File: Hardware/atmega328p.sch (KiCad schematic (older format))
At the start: 21 parts, among them J401 USART, Q001 Q_NPN_Darlington_BEC, U401 ATMEGA328P-PU, Y401 16MHz

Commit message: Atualização do MIC19
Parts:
- added RV401: 1K, Potentiometer_THT:Potentiometer_Bourns_3296W_Vertical, symbol Device:R_POT_TRIM
- BZ1: renamed from BZ001; footprint (none) -> Buzzer_Beeper:Buzzer_12x9.5RM7.6
- C407: footprint (none) -> Capacitor_SMD:C_0805_2012Metric_Pad1.15x1.40mm_HandSolder
- D402: value BYC77 -> BYD77; footprint (none) -> Diode_SMD:D_MiniMELF_Handsoldering
- Q101: renamed from Q001; value Q_NPN_Darlington_BEC -> BCV27; footprint (none) -> Package_TO_SOT_SMD:SOT-23_Handsoldering
- R404, R405, R406: footprint (none) -> Resistor_SMD:R_0805_2012Metric_Pad1.15x1.40mm_HandSolder
- renumbered D402 to D403
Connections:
- net +5V: now also R406.1, RV401.3; no longer BZ1.2 (+), D402.1 (K)
- net GND: no longer D403.1 (K)
- net at R404.1, U401.13 (PD7): no longer R406.2
- net at D403.2 (A): now also R406.2; no longer R406.1
- net at BZ1.1 (-), D402.2 (A), Q101.3 (C): now also D403.1 (K), RV401.1
- net ON_OFF_PUMP renamed SW_EMERGENCIA
- net SW_MOTOR_ON renamed SW_ENGINE_ON
- new net: BZ1.2 (+), D402.1 (K), RV401.2
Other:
- moved on the sheet: BZ1, D402, D403, R406
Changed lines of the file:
@@
 $Descr A4 11693 8268
 encoding utf-8
-Sheet 3 5
+Sheet 6 6
 Title ""
 Date ""
@@
 F 3 "" H 6150 4350 50  0001 C CNN
 	1    6150 4350
-	0    -1   -1   0
-$EndComp
-$Comp
-L Device:LED_Small D402
-U 1 1 59FE5354
-P 5900 5500
-F 0 "D402" H 5850 5625 50  0000 L CNN
-F 1 "LED_RED" H 5800 5400 50  0000 L CNN
-F 2 "LED_SMD:LED_0805_2012Metric_Pad1.15x1.40mm_HandSolder" V 5900 5500 50  0001 C CNN
-F 3 "" V 5900 5500 50  0001 C CNN
-	1    5900 5500
 	0    -1   -1   0
 $EndComp
@@
 Wire Wire Line
 	3650 3050 3650 3150
-Wire Wire Line
-	5050 2950 4950 2950
-NoConn ~ 5050 2950
 Text Label 5300 2850 0    60   ~ 0
 MCP_INT
@@
 Wire Wire Line
 	4550 2250 4550 2150
-Text Label 5050 4650 0    50   ~ 0
-ON_OFF_PUMP
-Text HLabel 5600 4650 2    50   Output ~ 0
-ON_OFF_PUMP
-Wire Wire Line
-	4950 4650 5600 4650
 Wire Wire Line
 	5050 3650 4950 3650
 $Comp
-L Device:Q_NPN_Darlington_BEC Q001
+L Device:Q_NPN_Darlington_BEC Q101
 U 1 1 5CCA71DB
 P 5500 6350
-F 0 "Q001" V 5736 6350 50  0000 C CNN
-F 1 "Q_NPN_Darlington_BEC" V 5827 6350 50  0000 C CNN
-F 2 "" H 5700 6450 50  0001 C CNN
+F 0 "Q101" V 5736 6350 50  0000 C CNN
+F 1 "BCV27" V 5827 6350 50  0000 C CNN
+F 2 "Package_TO_SOT_SMD:SOT-23_Handsoldering" H 5700 6450 50  0001 C CNN
 F 3 "~" H 5500 6350 50  0001 C CNN
 	1    5500 6350
@@
 $EndComp
 $Comp
-L Device:Buzzer BZ001
+L Device:Buzzer BZ1
 U 1 1 5CCB1F93
-P 4700 6350
-F 0 "BZ001" H 4706 6025 50  0000 C CNN
-F 1 "Buzzer" H 4706 6116 50  0000 C CNN
-F 2 "" V 4675 6450 50  0001 C CNN
-F 3 "~" V 4675 6450 50  0001 C CNN
-	1    4700 6350
+P 4250 6350
+F 0 "BZ1" H 4256 6025 50  0000 C CNN
+F 1 "Buzzer" H 4256 6116 50  0000 C CNN
+F 2 "Buzzer_Beeper:Buzzer_12x9.5RM7.6" V 4225 6450 50  0001 C CNN
+F 3 "~" V 4225 6450 50  0001 C CNN
+	1    4250 6350
 	-1   0    0    1
 $EndComp
@@
 L Device:D D402
 U 1 1 5CCB20DF
-P 5075 6300
-F 0 "D402" V 5029 6379 50  0000 L CNN
-F 1 "BYC77" V 5120 6379 50  0000 L CNN
-F 2 "" H 5075 6300 50  0001 C CNN
-F 3 "~" H 5075 6300 50  0001 C CNN
-	1    5075 6300
+P 4700 6300
+F 0 "D402" V 4654 6379 50  0000 L CNN
+F 1 "BYD77" V 4745 6379 50  0000 L CNN
+F 2 "Diode_SMD:D_MiniMELF_Handsoldering" H 4700 6300 50  0001 C CNN
+F 3 "~" H 4700 6300 50  0001 C CNN
+	1    4700 6300
 	0    1    1    0
 $EndComp
 Wire Wire Line
 	4350 5450 4350 5750
-Wire Wire Line
-	4800 6450 5075 6450
-Wire Wire Line
-	5075 6150 4950 6150
-Wire Wire Line
-	4950 6150 4950 6250
-Wire Wire Line
-	4950 6250 4800 6250
-$Comp
-L power:+5V #PWR?
+$Comp
+L power:+5V #PWR0108
 U 1 1 5CCB9AFA
-P 5075 6125
-F 0 "#PWR?" H 5075 5975 50  0001 C CNN
-F 1 "+5V" H 5125 6325 50  0000 C CNN
-F 2 "" H 5075 6125 50  0001 C CNN
-F 3 "" H 5075 6125 50  0001 C CNN
-	1    5075 6125
-	1    0    0    -1
-$EndComp
-Wire Wire Line
-	5075 6150 5075 6125
-Connection ~ 5075 6150
-Wire Wire Line
-	5075 6450 5300 6450
-Connection ~ 5075 6450
+P 4825 5750
+F 0 "#PWR0108" H 4825 5600 50  0001 C CNN
+F 1 "+5V" H 4875 5950 50  0000 C CNN
+F 2 "" H 4825 5750 50  0001 C CNN
+F 3 "" H 4825 5750 50  0001 C CNN
+	1    4825 5750
+	1    0    0    -1
+$EndComp
 Wire Wire Line
 	5500 6150 5500 6100
@@
 F 0 "R404" V 5400 5275 50  0000 L CNN
 F 1 "100R" V 5400 5025 50  0000 L CNN
-F 2 "" H 5500 5325 50  0001 C CNN
+F 2 "Resistor_SMD:R_0805_2012Metric_Pad1.15x1.40mm_HandSolder" H 5500 5325 50  0001 C CNN
 F 3 "~" H 5500 5325 50  0001 C CNN
 	1    5500 5325
@@
 F 0 "C407" V 5471 6100 50  0000 C CNN
 F 1 "100nF" V 5562 6100 50  0000 C CNN
-F 2 "" H 5700 6100 50  0001 C CNN
+F 2 "Capacitor_SMD:C_0805_2012Metric_Pad1.15x1.40mm_HandSolder" H 5700 6100 50  0001 C CNN
 F 3 "~" H 5700 6100 50  0001 C CNN
 	1    5700 6100
@@
 F 0 "R405" V 5625 5575 50  0000 L CNN
 F 1 "100R" V 5775 5575 50  0000 L CNN
-F 2 "" H 5700 5675 50  0001 C CNN
+F 2 "Resistor_SMD:R_0805_2012Metric_Pad1.15x1.40mm_HandSolder" H 5700 5675 50  0001 C CNN
 F 3 "~" H 5700 5675 50  0001 C CNN
 	1    5700 5675
@@
 Wire Wire Line
 	5800 5675 5900 5675
-Connection ~ 5900 5675
-Wire Wire Line
-	5900 5675 5900 5600
-$Comp
-L power:GND #PWR?
+$Comp
+L power:GND #PWR0109
 U 1 1 5CC9294B
 P 5900 6475
-F 0 "#PWR?" H 5900 6225 50  0001 C CNN
+F 0 "#PWR0109" H 5900 6225 50  0001 C CNN
 F 1 "GND" H 5905 6302 50  0000 C CNN
 F 2 "" H 5900 6475 50  0001 C CNN
@@
 L Device:R_Small R406
 U 1 1 5CCAD44D
-P 5700 5150
-F 0 "R406" V 5850 5150 50  0000 C CNN
-F 1 "330" V 5775 5150 50  0000 C CNN
-F 2 "" H 5700 5150 50  0001 C CNN
-F 3 "~" H 5700 5150 50  0001 C CNN
-	1    5700 5150
-	0    1    1    0
-$EndComp
-Wire Wire Line
-	5500 5150 5600 5150
-Connection ~ 5500 5150
-Wire Wire Line
-	5800 5150 5900 5150
-Wire Wire Line
-	5900 5150 5900 5400
+P 5200 5925
+F 0 "R406" V 5275 6150 50  0000 C CNN
+F 1 "330" V 5200 6125 50  0000 C CNN
+F 2 "Resistor_SMD:R_0805_2012Metric_Pad1.15x1.40mm_HandSolder" H 5200 5925 50  0001 C CNN
+F 3 "~" H 5200 5925 50  0001 C CNN
+	1    5200 5925
+	1    0    0    -1
+$EndComp
 Wire Wire Line
 	5900 6100 5900 6450
@@
 SW_BOAT_ON
 Text HLabel 5050 4850 2    50   Input ~ 0
-SW_MOTOR_ON
+SW_ENGINE_ON
 Text HLabel 5050 4950 2    50   Input ~ 0
 SW_MPPT_ON
 Text HLabel 5050 5050 2    50   Input ~ 0
 SW_DMS
+$Comp
+L Device:LED_Small D403
+U 1 1 59FE5354
+P 5200 6150
+F 0 "D403" H 5125 5975 50  0000 L CNN
+F 1 "LED_RED" H 5100 6050 50  0000 L CNN
+F 2 "LED_SMD:LED_0805_2012Metric_Pad1.15x1.40mm_HandSolder" V 5200 6150 50  0001 C CNN
+F 3 "" V 5200 6150 50  0001 C CNN
+	1    5200 6150
+	0    -1   -1   0
+$EndComp
+Wire Wire Line
+	5200 6025 5200 6050
+Wire Wire Line
+	5200 6250 5200 6450
+Connection ~ 5200 6450
+Wire Wire Line
+	5200 6450 5300 6450
+Text HLabel 5050 4650 2    50   Input ~ 0
+SW_EMERGENCIA
+NoConn ~ 4950 2950
+Wire Wire Line
+	4950 4650 5050 4650
+$Comp
+L Device:R_POT_TRIM RV401
+U 1 1 5CE256BF
+P 4825 5975
+F 0 "RV401" H 4756 5929 50  0000 R CNN
+F 1 "1K" H 4756 6020 50  0000 R CNN
+F 2 "Potentiometer_THT:Potentiometer_Bourns_3296W_Vertical" H 4825 5975 50  0001 C CNN
+F 3 "~" H 4825 5975 50  0001 C CNN
+	1    4825 5975
+	-1   0    0    1
+$EndComp
+Wire Wire Line
+	4825 5750 4825 5800
+Wire Wire Line
+	5200 5825 5200 5800
+Wire Wire Line
+	5200 5800 4825 5800
+Connection ~ 4825 5800
+Wire Wire Line
+	4825 5800 4825 5825
+Wire Wire Line
+	4350 6450 4700 6450
+Wire Wire Line
+	4350 6250 4600 6250
+Wire Wire Line
+	4600 6250 4600 6150
+Wire Wire Line
+	4600 5975 4675 5975
+Connection ~ 4700 6450
+Wire Wire Line
+	4700 6150 4600 6150
+Connection ~ 4600 6150
+Wire Wire Line
+	4600 6150 4600 5975
+Wire Wire Line
+	4825 6125 4825 6450
+Wire Wire Line
+	4700 6450 4825 6450
+Connection ~ 4825 6450
+Wire Wire Line
+	4825 6450 5200 6450
 $EndSCHEMATC

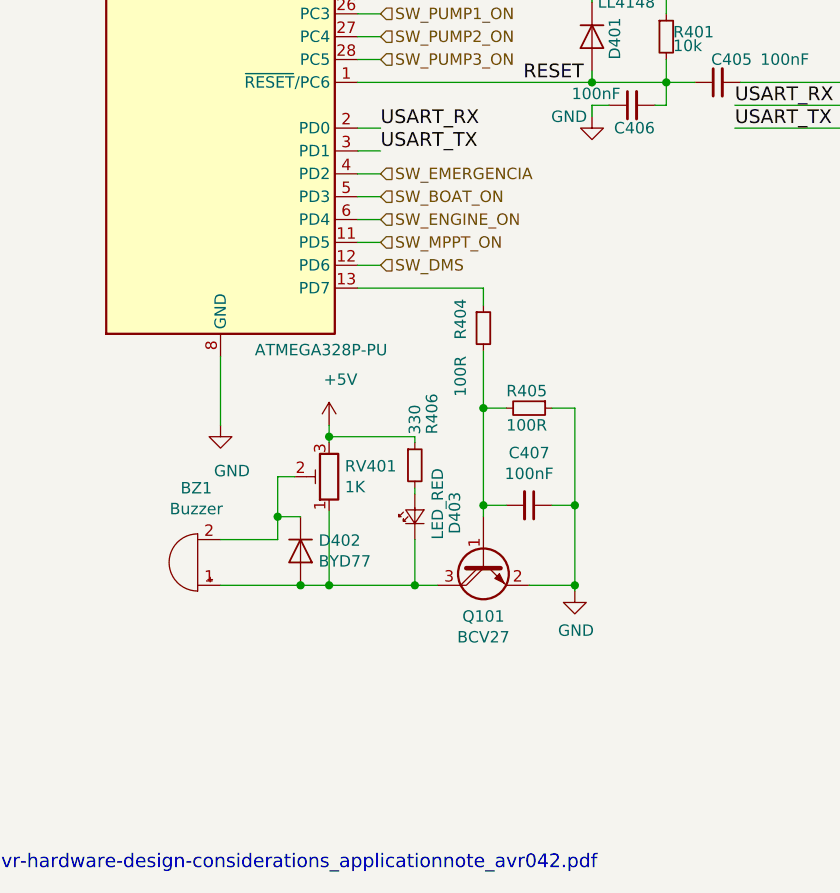
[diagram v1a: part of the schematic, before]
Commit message: Formato da placa modificado
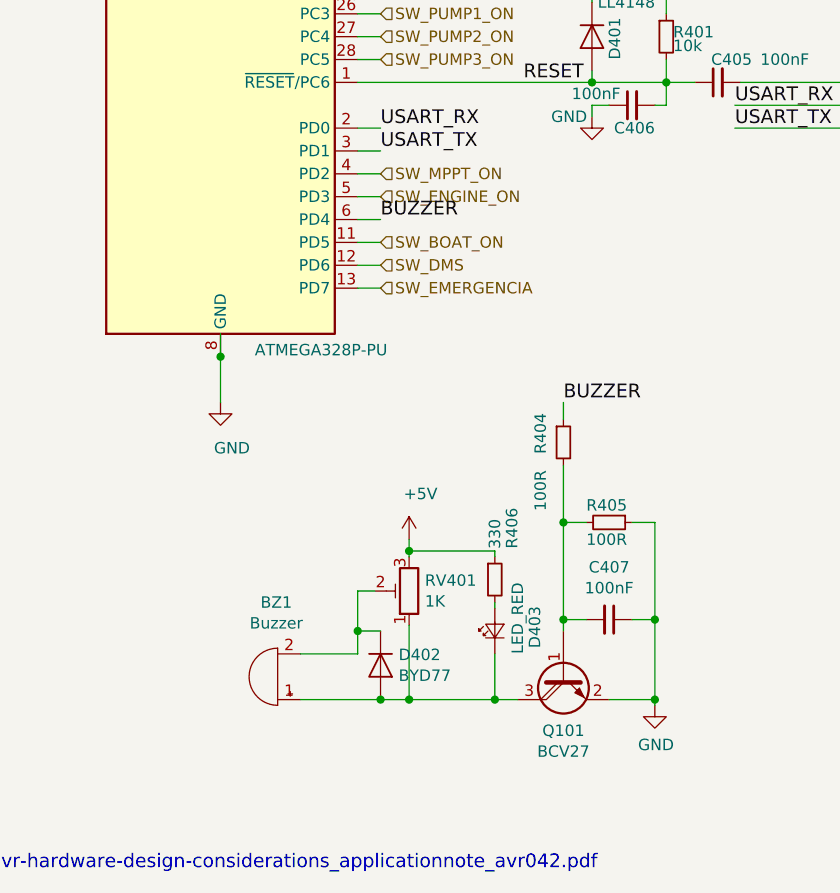
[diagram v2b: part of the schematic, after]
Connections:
- net SW_BOAT_ON: now also U401.11 (PD5); no longer U401.5 (PD3)
- net SW_EMERGENCIA: now also U401.13 (PD7); no longer U401.4 (PD2)
- net SW_ENGINE_ON: now also U401.5 (PD3); no longer U401.6 (PD4)
- net SW_MPPT_ON: now also U401.4 (PD2); no longer U401.11 (PD5)
- net BUZZER: now reaches R404.1
- net BUZZER: now also U401.6 (PD4); no longer U401.13 (PD7)
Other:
- moved on the sheet: BZ1, C407, D402, D403, Q101, R404, R405, R406, RV401
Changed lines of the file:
@@
 EESchema Schematic File Version 4
 LIBS:MIC19-cache
-EELAYER 26 0
+EELAYER 29 0
 EELAYER END
 $Descr A4 11693 8268
@@
 L power:GND #PWR0412
 U 1 1 5BEB7AB4
-P 4350 5750
-F 0 "#PWR0412" H 4350 5500 50  0001 C CNN
-F 1 "GND" H 4400 5550 50  0000 C CNN
-F 2 "" H 4350 5750 50  0001 C CNN
-F 3 "" H 4350 5750 50  0001 C CNN
-	1    4350 5750
+P 4350 5650
+F 0 "#PWR0412" H 4350 5400 50  0001 C CNN
+F 1 "GND" H 4400 5450 50  0000 C CNN
+F 2 "" H 4350 5650 50  0001 C CNN
+F 3 "" H 4350 5650 50  0001 C CNN
+	1    4350 5650
 	1    0    0    -1
 $EndComp
@@
 Wire Wire Line
 	4550 1850 4350 1850
-Wire Wire Line
-	4350 1850 4350 2350
 Connection ~ 4350 1850
 $Comp
@@
 L Device:Q_NPN_Darlington_BEC Q101
 U 1 1 5CCA71DB
-P 5500 6350
-F 0 "Q101" V 5736 6350 50  0000 C CNN
-F 1 "BCV27" V 5827 6350 50  0000 C CNN
-F 2 "Package_TO_SOT_SMD:SOT-23_Handsoldering" H 5700 6450 50  0001 C CNN
-F 3 "~" H 5500 6350 50  0001 C CNN
-	1    5500 6350
+P 5850 6850
+F 0 "Q101" V 6086 6850 50  0000 C CNN
+F 1 "BCV27" V 6177 6850 50  0000 C CNN
+F 2 "Package_TO_SOT_SMD:SOT-23_Handsoldering" H 6050 6950 50  0001 C CNN
+F 3 "~" H 5850 6850 50  0001 C CNN
+	1    5850 6850
 	0    -1   1    0
 $EndComp
@@
 L Device:Buzzer BZ1
 U 1 1 5CCB1F93
-P 4250 6350
-F 0 "BZ1" H 4256 6025 50  0000 C CNN
-F 1 "Buzzer" H 4256 6116 50  0000 C CNN
-F 2 "Buzzer_Beeper:Buzzer_12x9.5RM7.6" V 4225 6450 50  0001 C CNN
-F 3 "~" V 4225 6450 50  0001 C CNN
-	1    4250 6350
+P 4600 6850
+F 0 "BZ1" H 4606 6525 50  0000 C CNN
+F 1 "Buzzer" H 4606 6616 50  0000 C CNN
+F 2 "Buzzer_Beeper:Buzzer_12x9.5RM7.6" V 4575 6950 50  0001 C CNN
+F 3 "~" V 4575 6950 50  0001 C CNN
+	1    4600 6850
 	-1   0    0    1
 $EndComp
@@
 L Device:D D402
 U 1 1 5CCB20DF
-P 4700 6300
-F 0 "D402" V 4654 6379 50  0000 L CNN
-F 1 "BYD77" V 4745 6379 50  0000 L CNN
-F 2 "Diode_SMD:D_MiniMELF_Handsoldering" H 4700 6300 50  0001 C CNN
-F 3 "~" H 4700 6300 50  0001 C CNN
-	1    4700 6300
+P 5050 6800
+F 0 "D402" V 5004 6879 50  0000 L CNN
+F 1 "BYD77" V 5095 6879 50  0000 L CNN
+F 2 "Diode_SMD:D_MiniMELF_Handsoldering" H 5050 6800 50  0001 C CNN
+F 3 "~" H 5050 6800 50  0001 C CNN
+	1    5050 6800
 	0    1    1    0
 $EndComp
 Wire Wire Line
-	4350 5450 4350 5750
+	4350 5350 4350 5450
 $Comp
 L power:+5V #PWR0108
 U 1 1 5CCB9AFA
-P 4825 5750
-F 0 "#PWR0108" H 4825 5600 50  0001 C CNN
-F 1 "+5V" H 4875 5950 50  0000 C CNN
-F 2 "" H 4825 5750 50  0001 C CNN
-F 3 "" H 4825 5750 50  0001 C CNN
-	1    4825 5750
-	1    0    0    -1
-$EndComp
-Wire Wire Line
-	5500 6150 5500 6100
-Wire Wire Line
-	5500 6100 5600 6100
+P 5175 6250
+F 0 "#PWR0108" H 5175 6100 50  0001 C CNN
+F 1 "+5V" H 5225 6450 50  0000 C CNN
+F 2 "" H 5175 6250 50  0001 C CNN
+F 3 "" H 5175 6250 50  0001 C CNN
+	1    5175 6250
+	1    0    0    -1
+$EndComp
+Wire Wire Line
+	5850 6650 5850 6600
+Wire Wire Line
+	5850 6600 5950 6600
 $Comp
 L Device:R_Small R404
 U 1 1 5CC7EF01
-P 5500 5325
-F 0 "R404" V 5400 5275 50  0000 L CNN
-F 1 "100R" V 5400 5025 50  0000 L CNN
-F 2 "Resistor_SMD:R_0805_2012Metric_Pad1.15x1.40mm_HandSolder" H 5500 5325 50  0001 C CNN
-F 3 "~" H 5500 5325 50  0001 C CNN
-	1    5500 5325
+P 5850 5825
+F 0 "R404" V 5750 5775 50  0000 L CNN
+F 1 "100R" V 5750 5525 50  0000 L CNN
+F 2 "Resistor_SMD:R_0805_2012Metric_Pad1.15x1.40mm_HandSolder" H 5850 5825 50  0001 C CNN
+F 3 "~" H 5850 5825 50  0001 C CNN
+	1    5850 5825
 	1    0    0    -1
 $EndComp
@@
 L Device:C_Small C407
 U 1 1 5CC81983
-P 5700 6100
-F 0 "C407" V 5471 6100 50  0000 C CNN
-F 1 "100nF" V 5562 6100 50  0000 C CNN
-F 2 "Capacitor_SMD:C_0805_2012Metric_Pad1.15x1.40mm_HandSolder" H 5700 6100 50  0001 C CNN
-F 3 "~" H 5700 6100 50  0001 C CNN
-	1    5700 6100
+P 6050 6600
+F 0 "C407" V 5821 6600 50  0000 C CNN
+F 1 "100nF" V 5912 6600 50  0000 C CNN
+F 2 "Capacitor_SMD:C_0805_2012Metric_Pad1.15x1.40mm_HandSolder" H 6050 6600 50  0001 C CNN
+F 3 "~" H 6050 6600 50  0001 C CNN
+	1    6050 6600
 	0    1    1    0
 $EndComp
 Wire Wire Line
-	4950 5150 5500 5150
-Wire Wire Line
-	5500 5150 5500 5225
-Wire Wire Line
-	5500 5425 5500 5675
-Connection ~ 5500 6100
+	5850 5650 5850 5725
+Wire Wire Line
+	5850 5925 5850 6175
+Connection ~ 5850 6600
 $Comp
 L Device:R_Small R405
 U 1 1 5CC86858
-P 5700 5675
-F 0 "R405" V 5625 5575 50  0000 L CNN
-F 1 "100R" V 5775 5575 50  0000 L CNN
-F 2 "Resistor_SMD:R_0805_2012Metric_Pad1.15x1.40mm_HandSolder" H 5700 5675 50  0001 C CNN
-F 3 "~" H 5700 5675 50  0001 C CNN
-	1    5700 5675
+P 6050 6175
+F 0 "R405" V 5975 6075 50  0000 L CNN
+F 1 "100R" V 6125 6075 50  0000 L CNN
+F 2 "Resistor_SMD:R_0805_2012Metric_Pad1.15x1.40mm_HandSolder" H 6050 6175 50  0001 C CNN
+F 3 "~" H 6050 6175 50  0001 C CNN
+	1    6050 6175
 	0    1    1    0
 $EndComp
 Wire Wire Line
-	5600 5675 5500 5675
-Connection ~ 5500 5675
-Wire Wire Line
-	5500 5675 5500 6100
-Wire Wire Line
-	5700 6450 5900 6450
-Wire Wire Line
-	5800 6100 5900 6100
-Wire Wire Line
-	5900 6100 5900 5675
-Wire Wire Line
-	5800 5675 5900 5675
+	5950 6175 5850 6175
+Connection ~ 5850 6175
+Wire Wire Line
+	5850 6175 5850 6600
+Wire Wire Line
+	6050 6950 6250 6950
+Wire Wire Line
+	6150 6600 6250 6600
+Wire Wire Line
+	6250 6600 6250 6175
+Wire Wire Line
+	6150 6175 6250 6175
 $Comp
 L power:GND #PWR0109
 U 1 1 5CC9294B
-P 5900 6475
-F 0 "#PWR0109" H 5900 6225 50  0001 C CNN
-F 1 "GND" H 5905 6302 50  0000 C CNN
-F 2 "" H 5900 6475 50  0001 C CNN
-F 3 "" H 5900 6475 50  0001 C CNN
-	1    5900 6475
-	1    0    0    -1
-$EndComp
-Wire Wire Line
-	5900 6475 5900 6450
+P 6250 6975
+F 0 "#PWR0109" H 6250 6725 50  0001 C CNN
+F 1 "GND" H 6255 6802 50  0000 C CNN
+F 2 "" H 6250 6975 50  0001 C CNN
+F 3 "" H 6250 6975 50  0001 C CNN
+	1    6250 6975
+	1    0    0    -1
+$EndComp
+Wire Wire Line
+	6250 6975 6250 6950
 $Comp
 L Device:R_Small R406
 U 1 1 5CCAD44D
-P 5200 5925
-F 0 "R406" V 5275 6150 50  0000 C CNN
-F 1 "330" V 5200 6125 50  0000 C CNN
-F 2 "Resistor_SMD:R_0805_2012Metric_Pad1.15x1.40mm_HandSolder" H 5200 5925 50  0001 C CNN
-F 3 "~" H 5200 5925 50  0001 C CNN
-	1    5200 5925
-	1    0    0    -1
-$EndComp
-Wire Wire Line
-	5900 6100 5900 6450
-Connection ~ 5900 6100
-Connection ~ 5900 6450
+P 5550 6425
+F 0 "R406" V 5625 6650 50  0000 C CNN
+F 1 "330" V 5550 6625 50  0000 C CNN
+F 2 "Resistor_SMD:R_0805_2012Metric_Pad1.15x1.40mm_HandSolder" H 5550 6425 50  0001 C CNN
+F 3 "~" H 5550 6425 50  0001 C CNN
+	1    5550 6425
+	1    0    0    -1
+$EndComp
+Wire Wire Line
+	6250 6600 6250 6950
+Connection ~ 6250 6600
+Connection ~ 6250 6950
 Wire Wire Line
 	4950 4950 5050 4950
@@
 	6300 4250 5975 4250
 Connection ~ 5975 4250
+Text HLabel 5050 4950 2    50   Input ~ 0
+SW_BOAT_ON
 Text HLabel 5050 4750 2    50   Input ~ 0
-SW_BOAT_ON
-Text HLabel 5050 4850 2    50   Input ~ 0
 SW_ENGINE_ON
-Text HLabel 5050 4950 2    50   Input ~ 0
+Text HLabel 5050 4650 2    50   Input ~ 0
 SW_MPPT_ON
 Text HLabel 5050 5050 2    50   Input ~ 0
@@
 L Device:LED_Small D403
 U 1 1 59FE5354
-P 5200 6150
-F 0 "D403" H 5125 5975 50  0000 L CNN
-F 1 "LED_RED" H 5100 6050 50  0000 L CNN
-F 2 "LED_SMD:LED_0805_2012Metric_Pad1.15x1.40mm_HandSolder" V 5200 6150 50  0001 C CNN
-F 3 "" V 5200 6150 50  0001 C CNN
-	1    5200 6150
+P 5550 6650
+F 0 "D403" H 5475 6475 50  0000 L CNN
+F 1 "LED_RED" H 5450 6550 50  0000 L CNN
+F 2 "LED_SMD:LED_0805_2012Metric_Pad1.15x1.40mm_HandSolder" V 5550 6650 50  0001 C CNN
+F 3 "" V 5550 6650 50  0001 C CNN
+	1    5550 6650
 	0    -1   -1   0
 $EndComp
 Wire Wire Line
-	5200 6025 5200 6050
-Wire Wire Line
-	5200 6250 5200 6450
-Connection ~ 5200 6450
-Wire Wire Line
-	5200 6450 5300 6450
-Text HLabel 5050 4650 2    50   Input ~ 0
+	5550 6525 5550 6550
+Wire Wire Line
+	5550 6750 5550 6950
+Connection ~ 5550 6950
+Wire Wire Line
+	5550 6950 5650 6950
+Text HLabel 5050 5150 2    50   Input ~ 0
 SW_EMERGENCIA
 NoConn ~ 4950 2950
@@
 L Device:R_POT_TRIM RV401
 U 1 1 5CE256BF
-P 4825 5975
-F 0 "RV401" H 4756 5929 50  0000 R CNN
-F 1 "1K" H 4756 6020 50  0000 R CNN
-F 2 "Potentiometer_THT:Potentiometer_Bourns_3296W_Vertical" H 4825 5975 50  0001 C CNN
-F 3 "~" H 4825 5975 50  0001 C CNN
-	1    4825 5975
+P 5175 6475
+F 0 "RV401" H 5106 6429 50  0000 R CNN
+F 1 "1K" H 5106 6520 50  0000 R CNN
+F 2 "Potentiometer_THT:Potentiometer_Bourns_3296W_Vertical" H 5175 6475 50  0001 C CNN
+F 3 "~" H 5175 6475 50  0001 C CNN
+	1    5175 6475
 	-1   0    0    1
 $EndComp
 Wire Wire Line
-	4825 5750 4825 5800
-Wire Wire Line
-	5200 5825 5200 5800
-Wire Wire Line
-	5200 5800 4825 5800
-Connection ~ 4825 5800
-Wire Wire Line
-	4825 5800 4825 5825
-Wire Wire Line
-	4350 6450 4700 6450
-Wire Wire Line
-	4350 6250 4600 6250
-Wire Wire Line
-	4600 6250 4600 6150
-Wire Wire Line
-	4600 5975 4675 5975
-Connection ~ 4700 6450
-Wire Wire Line
-	4700 6150 4600 6150
-Connection ~ 4600 6150
-Wire Wire Line
-	4600 6150 4600 5975
-Wire Wire Line
-	4825 6125 4825 6450
-Wire Wire Line
-	4700 6450 4825 6450
-Connection ~ 4825 6450
-Wire Wire Line
-	4825 6450 5200 6450
+	5175 6250 5175 6300
+Wire Wire Line
+	5550 6325 5550 6300
+Wire Wire Line
+	5550 6300 5175 6300
+Connection ~ 5175 6300
+Wire Wire Line
+	5175 6300 5175 6325
+Wire Wire Line
+	4700 6950 5050 6950
+Wire Wire Line
+	4700 6750 4950 6750
+Wire Wire Line
+	4950 6750 4950 6650
+Wire Wire Line
+	4950 6475 5025 6475
+Connection ~ 5050 6950
+Wire Wire Line
+	5050 6650 4950 6650
+Connection ~ 4950 6650
+Wire Wire Line
+	4950 6650 4950 6475
+Wire Wire Line
+	5175 6625 5175 6950
+Wire Wire Line
+	5050 6950 5175 6950
+Connection ~ 5175 6950
+Wire Wire Line
+	5175 6950 5550 6950
+Text Label 5050 4850 0    60   ~ 0
+BUZZER
+Text Label 5850 5650 0    60   ~ 0
+BUZZER
+Connection ~ 4350 5450
+Wire Wire Line
+	4350 5450 4350 5650
+Wire Wire Line
+	5050 5150 4950 5150
+Wire Wire Line
+	4350 1850 4350 2350
 $EndSCHEMATC
